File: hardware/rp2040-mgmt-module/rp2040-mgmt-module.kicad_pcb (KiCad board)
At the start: 2 copper layers, 77 x 24 mm, 86 parts, among them J1 SWD, J2 Bus_PCI_Express_x1, J3 USB_B_Micro, J4 RJ45_Hanrun_HR913550A_Horizon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, J5 ADC, J6 UART, J7 UART, SW1 BOOT, SW2 RESET, U1 W5500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

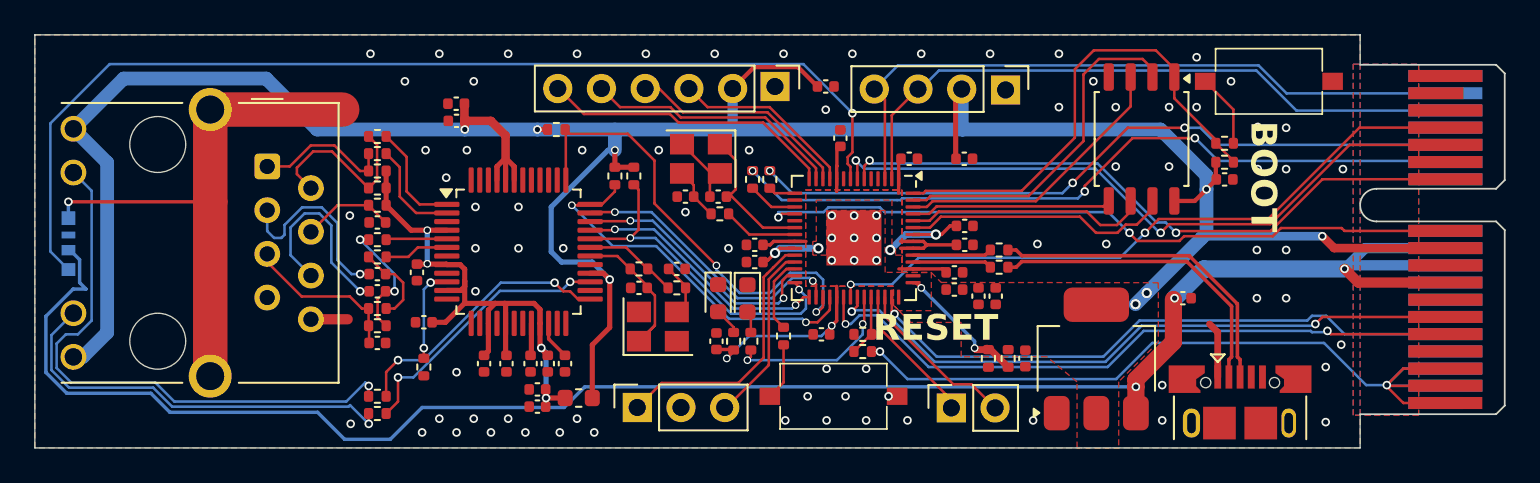
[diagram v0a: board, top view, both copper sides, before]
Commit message: fix: can't forget the pull-ups
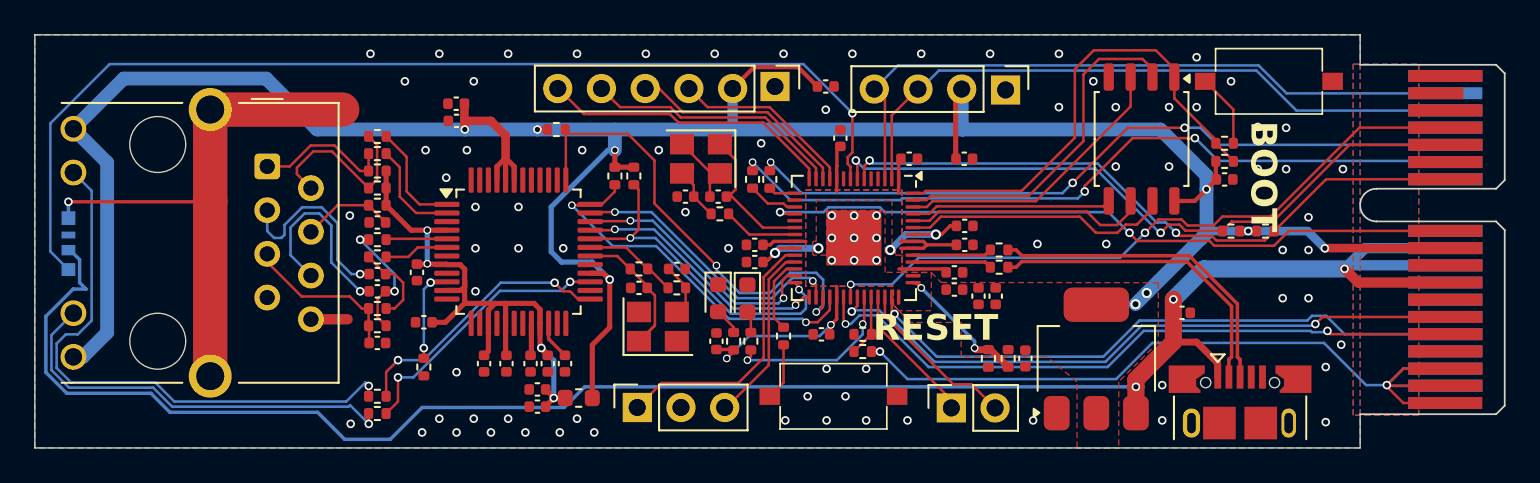
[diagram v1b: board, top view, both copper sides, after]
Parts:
- added R32: 4.7K, Resistor_SMD:R_0402_1005Metric, F.Cu at (119.5, 58.4)
- added R33: 4.7K, Resistor_SMD:R_0402_1005Metric, F.Cu at (117.5, 58.4)
- moved C19 0.85 mm to (114.7, 63.1)
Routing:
- net +3.3V: track 184.8 -> 186.0 mm, vias 10 -> 11
- net +5V: track 115.0 -> 115.8 mm
- net /DIO: track 43.2 -> 43.9 mm
- net /CLK: track 41.8 -> 42.4 mm
